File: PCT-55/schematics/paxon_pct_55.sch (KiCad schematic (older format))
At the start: 546 parts, among them IC201 HA11431, IC202 TA7676AP, IC301 HA11423, IC502 _, IC901 TC4052BP, IC902 TC4052BP, IC950 HD7407, J401 CONN_01x05, J403 CONN_01x04, J404 CONN_01x07, J503 CONN_01x04, J503-1 CONN_01x04, J505 CONN_01x02, J903 CONN_01x02, J913 CONN_01x05, J918 CONN_01x02, J919 CONN_01x04, J920 CONN_01x08, J921 CONN_01x06, J927 CONN_01x03, K1 CONN_01x03, P402 CONN_01x03, P504 CONN_01x09, P801 CONN_01x03, P802 CONN_01x03, P901 CONN_01x09, P902 CONN_01x06, P903 CONN_01x02, P911 CONN_01x05, P912 CONN_01x02, P913 CONN_01x05, P914 CONN_01x04, P917 CONN_01x02, P918 CONN_01x02, P919 CONN_01x04, P927 CONN_01x03, Q202 A854_PNP_BCE, Q203 A1015_PNP_BCE, Q204 A1015_PNP_BCE, Q301 C2073_NPN_BCE, Q302 C2073_NPN_BCE, Q303 A1015_PNP_BCE, Q304 C1815_NPN_BCE, Q351 C2610_NPN_BCE, Q352 D1425_NPN_BCE, Q451 D758_NPN_BCE, Q452 D758_NPN_BCE, Q453 D758_NPN_BCE, Q454 C1815_NPN_BCE, Q455 C1815_NPN_BCE, Q456 C1815_NPN_BCE, Q501 A1015_PNP_BCE, Q502 C1815_NPN_BCE, Q503 C2236_NPN_CBE, Q504 2SC2122A_NPN_BCE, Q505 D1052A_NPN_BCE, Q551 A733_PNP_BCE, Q801 C1815_NPN_BCE, Q802 A950_PNP_BCE, Q803 C2120_NPN_BCE, Q901 A952_PNP_BCE, Q902 C1815_NPN_BCE, Q903 A733_PNP_BCE, Q905 ???, Q906 ???, Q950 C1815_NPN_BCE, Q951 A950_PNP_BCE, Q952 C2120_NPN_BCE, Q953 C1815_NPN_BCE, Q954 C1815_NPN_BCE, Q955 C1815_NPN_BCE, SW1 CH1, SW10 MSX, SW2 CH2, SW3 CH3, SW4 CH4, SW5 CH5, SW6 CH6, SW7 CH7, SW8 CH8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

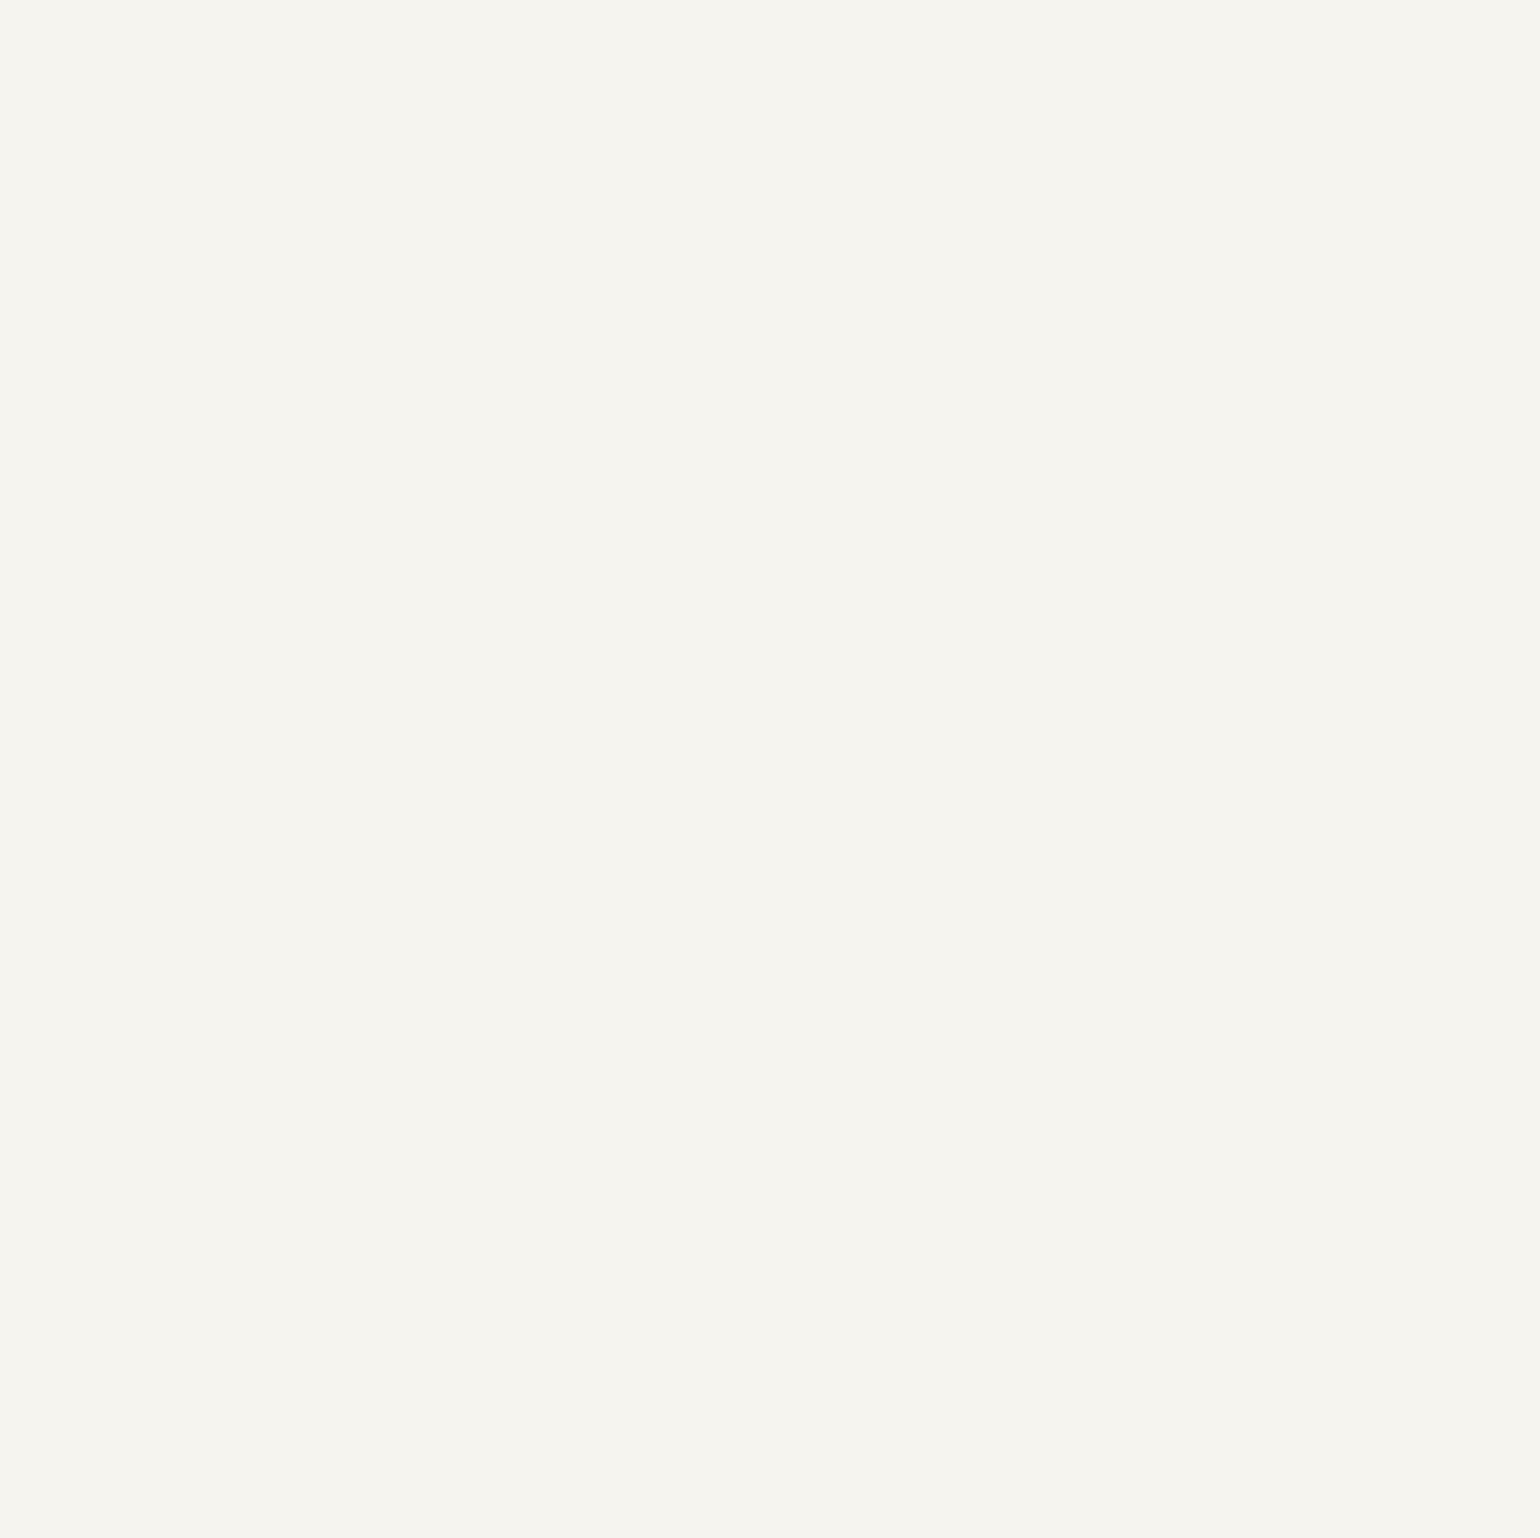
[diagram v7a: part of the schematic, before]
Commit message: added IF box schematics
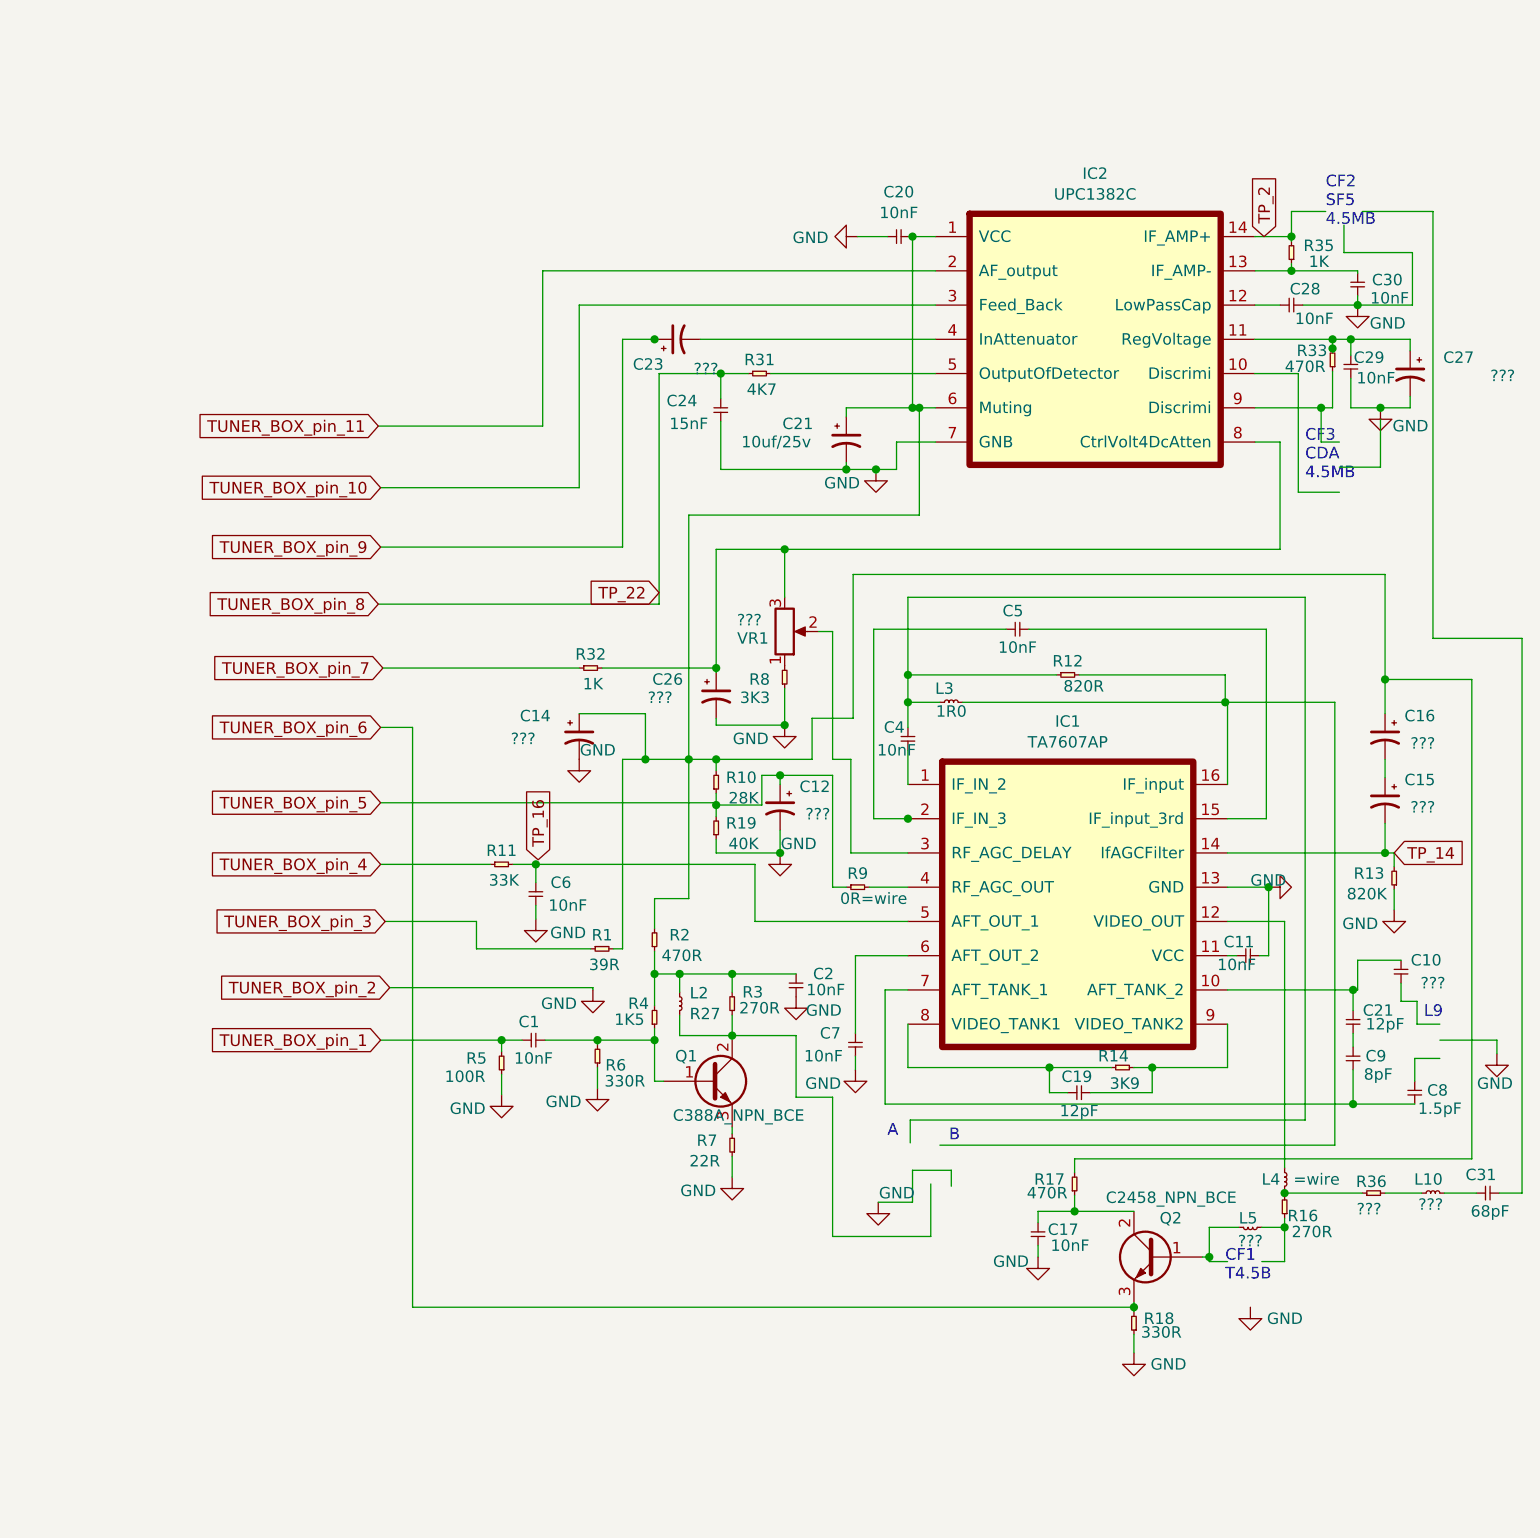
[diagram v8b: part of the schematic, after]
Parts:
- added C1, C11, C17, C2, C20, C28, C29, C30, C4, C5, C6, C7: 10nF, symbol agg-kicad:C
- added C10: ???, symbol agg-kicad:C
- added C12, C14, C15, C16, C23, C26, C27: ???, symbol Device:CP1_Small
- added C19, C21: 12pF, symbol agg-kicad:C
- added C21: 10uf/25v, symbol Device:CP1_Small
- added C24: 15nF, symbol agg-kicad:C
- added C31: 68pF, symbol agg-kicad:C
- added C8: 1.5pF, symbol agg-kicad:C
- added C9: 8pF, symbol agg-kicad:C
- added IC1: TA7607AP, symbol Video:TA7607AP
- added IC2: UPC1382C, symbol Video:UPC1382C
- added L10, L5: ???, symbol agg-kicad:L
- added L2: R27, symbol agg-kicad:L
- added L3: 1R0, symbol agg-kicad:L
- added L4: =wire, symbol agg-kicad:L
- added Q1: C388A_NPN_BCE, symbol Device:Q_NPN_BCE
- added Q2: C2458_NPN_BCE, symbol Device:Q_NPN_BCE
- added R1: 39R, symbol agg-kicad:R
- added R10: 28K, symbol agg-kicad:R
- added R11: 33K, symbol agg-kicad:R
- added R12: 820R, symbol agg-kicad:R
- added R13: 820K, symbol agg-kicad:R
- added R14: 3K9, symbol agg-kicad:R
- added R16, R3: 270R, symbol agg-kicad:R
- added R17, R2, R33: 470R, symbol agg-kicad:R
- added R18, R6: 330R, symbol agg-kicad:R
- added R19: 40K, symbol agg-kicad:R
- added R31: 4K7, symbol agg-kicad:R
- added R32, R35: 1K, symbol agg-kicad:R
- added R36: ???, symbol agg-kicad:R
- added R4: 1K5, symbol agg-kicad:R
- added R5: 100R, symbol agg-kicad:R
- added R7: 22R, symbol agg-kicad:R
- added R8: 3K3, symbol agg-kicad:R
- added R9: 0R=wire, symbol agg-kicad:R
- added VR1: ???, symbol Device:R_POT
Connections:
- net labels added: TP_14, TP_16, TP_2, TP_22, TUNER_BOX_pin_1, TUNER_BOX_pin_10, TUNER_BOX_pin_11, TUNER_BOX_pin_2, TUNER_BOX_pin_3, TUNER_BOX_pin_4, TUNER_BOX_pin_5, TUNER_BOX_pin_6, TUNER_BOX_pin_7, TUNER_BOX_pin_8, TUNER_BOX_pin_9
- wire segments 2158 -> 2429
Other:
- note added: "A"
- note added: "B"
- note added: "CF1\nT4.5B"
- note added: "CF2 \nSF5\n4.5MB"
- note added: "CF3\nCDA\n4.5MB"
- note added: "L9"
